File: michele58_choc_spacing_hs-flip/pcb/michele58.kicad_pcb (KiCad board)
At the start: 2 copper layers, 143.6 x 107.9 mm, 115 parts, among them J1 OLED, J2 i2c, J3 i2c, J4 LED, U1 Elite-Pi_RP2040, U2 TRRS

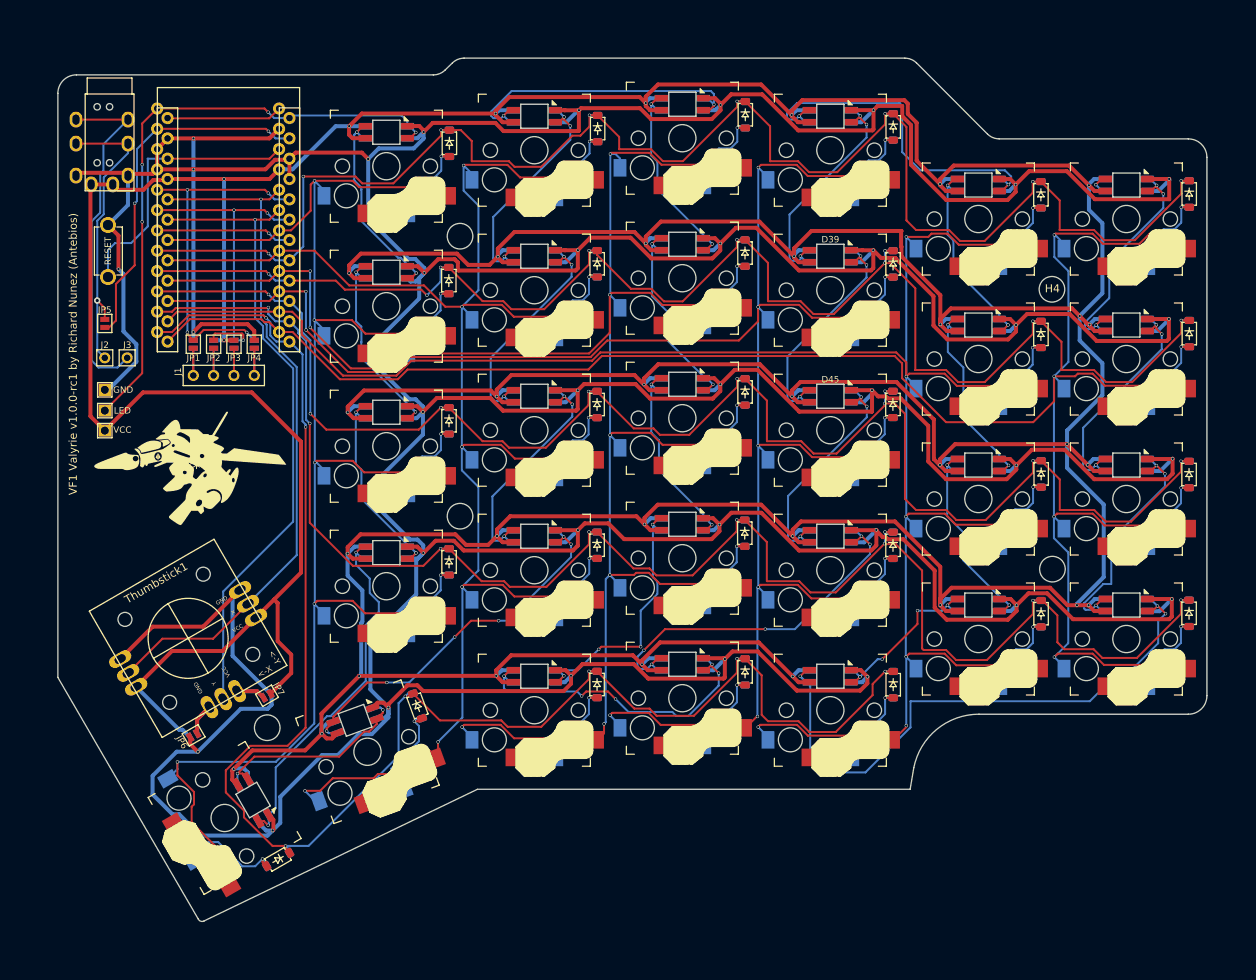
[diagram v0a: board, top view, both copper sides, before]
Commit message: Made mounting holes larger, added mask, and add STL for bottom case with spacers.
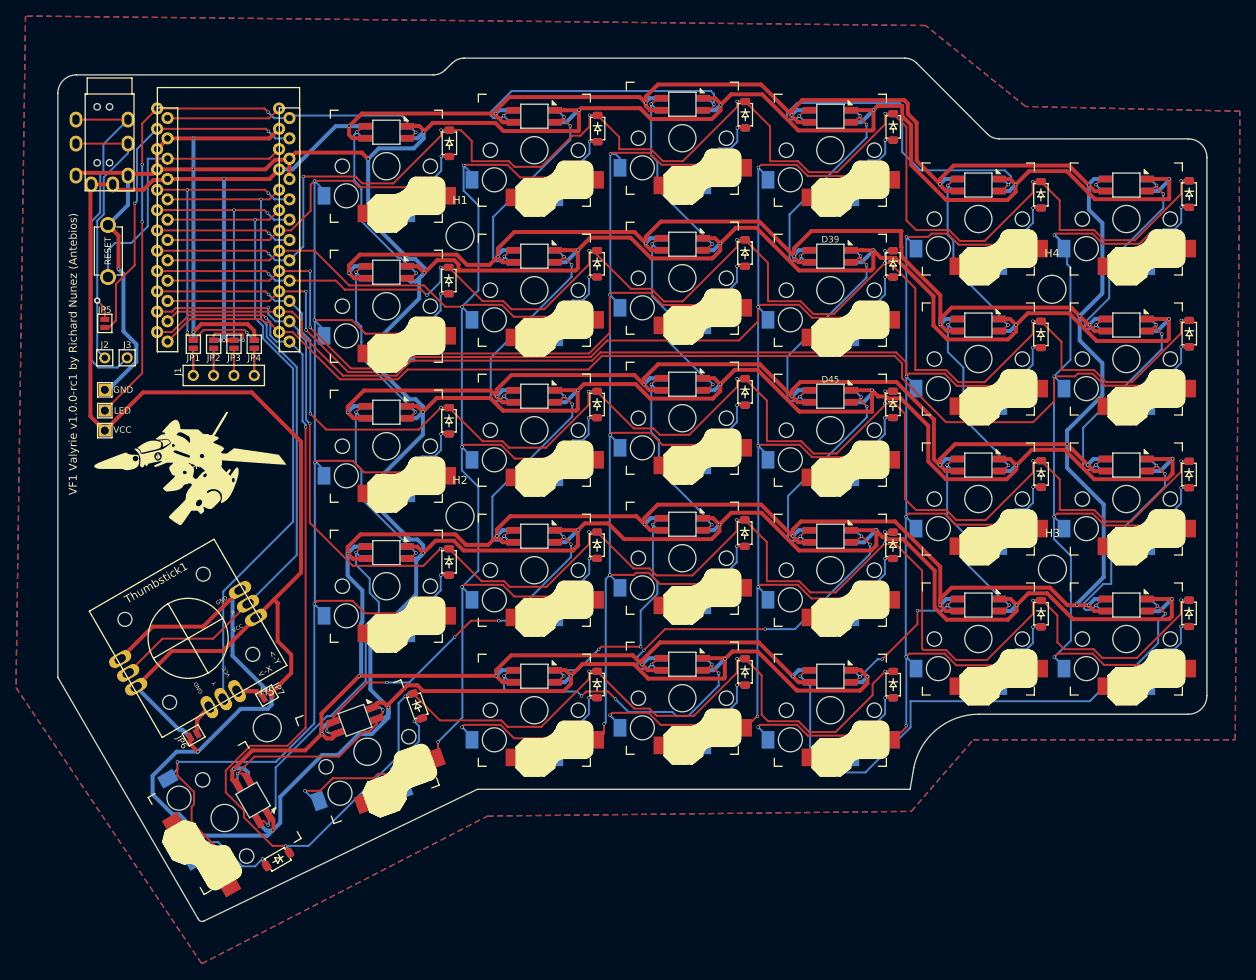
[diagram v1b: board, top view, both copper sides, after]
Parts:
- H1, H2, H3, H4, H5: footprint MountingHole:MountingHole_3.2mm_M3 -> MountingHole:MountingHole_3.5mm
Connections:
- JP1 pad 1: Net-(J1-P4) -> Net-(J1-P1)
- JP2 pad 1: Net-(J1-P3) -> Net-(J1-P2)
- JP3 pad 1: Net-(J1-P2) -> Net-(J1-P3)
- JP4 pad 1: Net-(J1-P1) -> Net-(J1-P4)
- JP6 pad 2: VCC -> GND
- JP7 pad 1: VCC -> Net-(JP7-A)
- JP7 pad 2: Net-(JP7-A) -> VCC (x2)
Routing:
- added copper zone on B.Cu, net (none)
- added copper zone on F.Cu, net (none)
